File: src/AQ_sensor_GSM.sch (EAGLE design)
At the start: 56 parts, among them IC2 MCP73831/OT, J1 F-1X03-SIP-100-32, SW1 PCM12SMTR, U2 TEXAS_INSTRUMENTS_SN74HC125TE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, U3 TEXAS_INSTRUMENTS_LM1117IMP-3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, U4 ESP8266-12E/ESP-12E, U5 CH340G, X1 53048-08, X2 SIMLOCK-C707_10M006_512_2, X4 50 Ohms

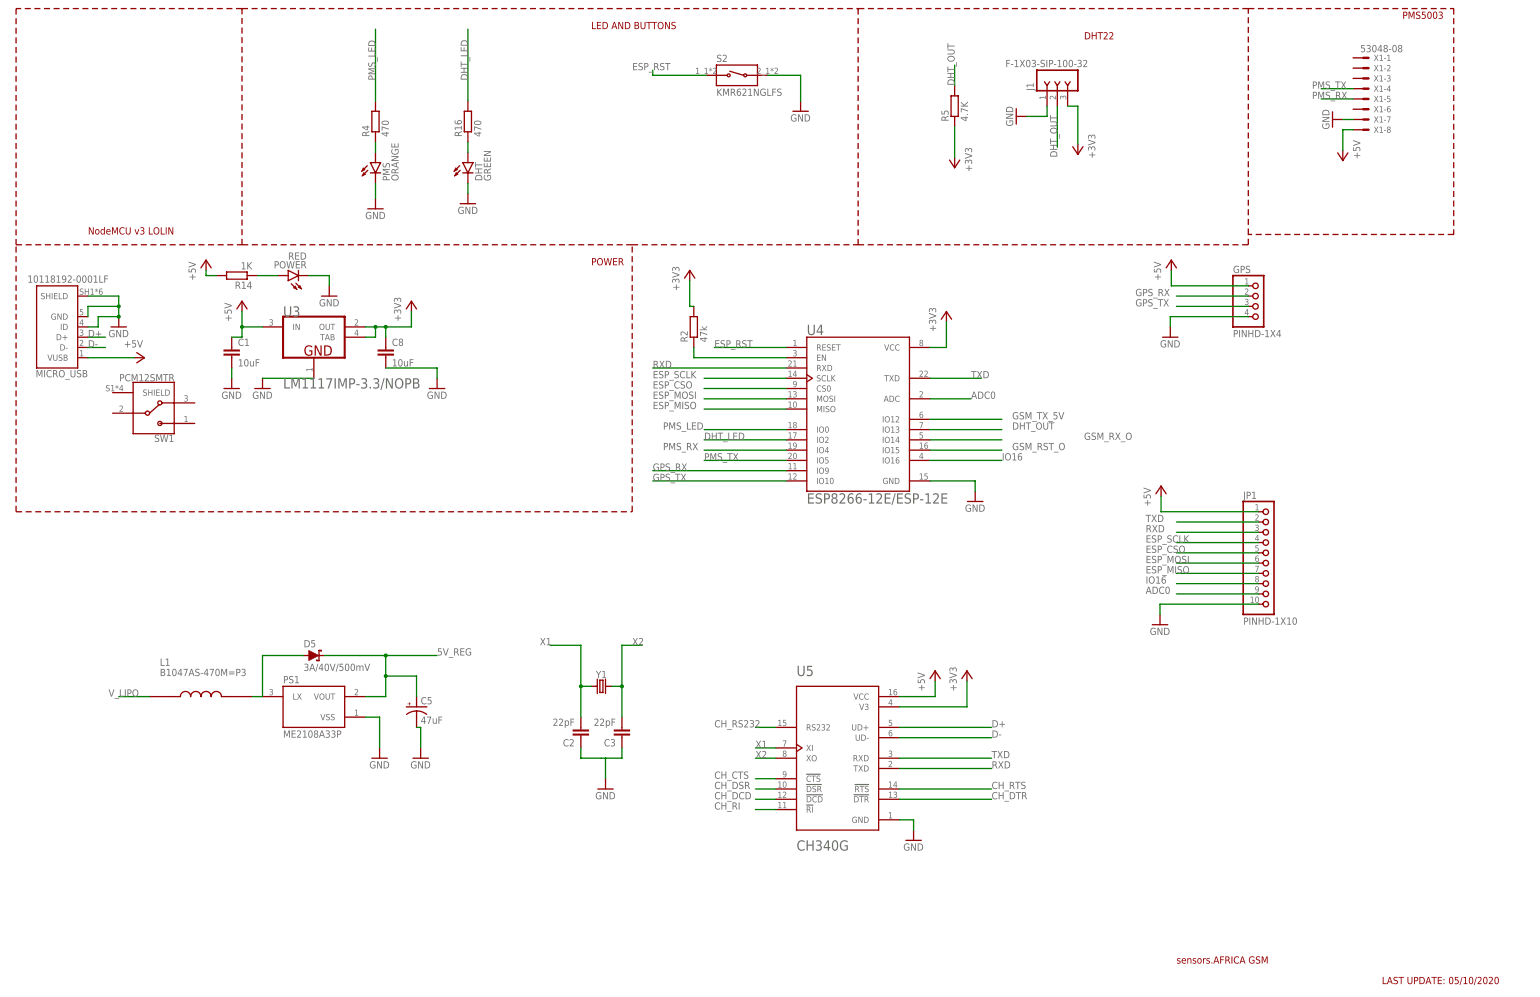
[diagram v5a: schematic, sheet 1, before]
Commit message: Changed Lipo charging IC to TP4056. Added Power Switch to the lipo Circuitry
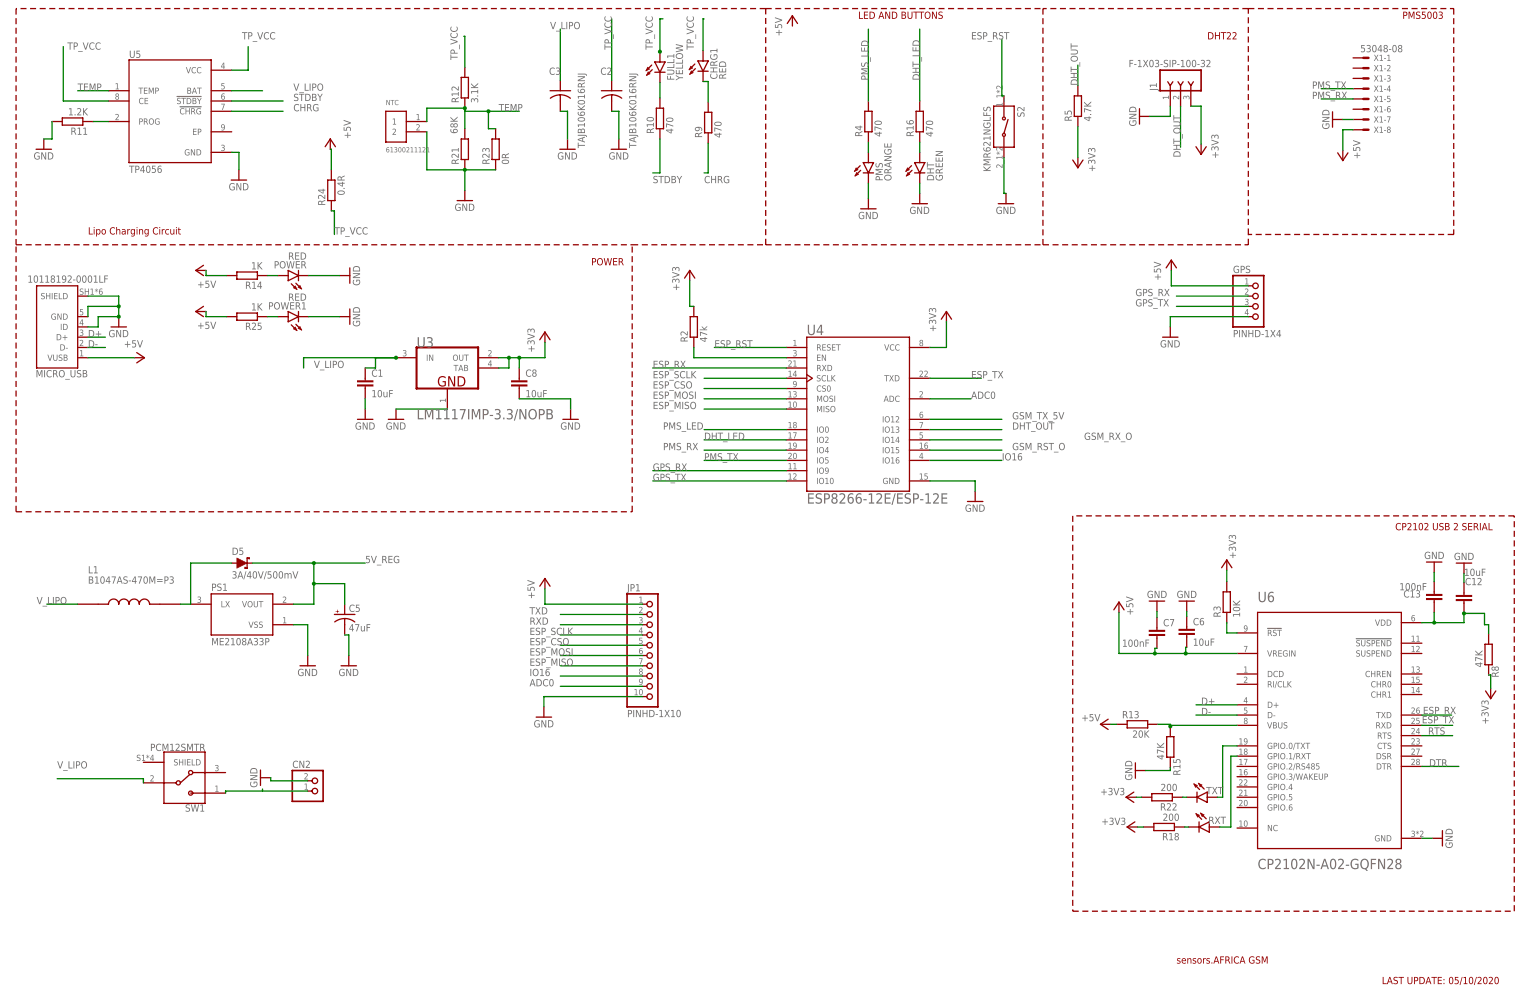
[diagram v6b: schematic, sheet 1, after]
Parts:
- removed Y1: (no value), SparkFun-Clocks:CRYSTALPTH-HC49US
- added C12, C6: 10uF, rcl:C-EUC0603
- added C13, C7: 100nF, rcl:C-EUC0805
- added CHRG1, POWER1: RED, led:LEDCHIP-LED0603
- added CN2: (no value), AQ_sensor_GSM:JST_2PIN-SMT-RA
- added FULL1: YELLOW, led:LEDCHIP-LED0603
- added NTC: 61300211121, Headers:61300211121
- added R10, R9: 470, rcl:R-EU_R0603
- added R11: 1.2K, rcl:R-EU_R0603
- added R12: 3.1K, rcl:R-EU_R0603
- added R13: 20K, rcl:R-EU_R0603
- added R15, R8: 47K, rcl:R-EU_R0603
- added R18, R22: 200, rcl:R-EU_R0603
- added R21: 68K, rcl:R-EU_R0603
- added R23: 0R, rcl:R-EU_R0603
- added R24: 0.4R, rcl:R-EU_R0603
- added R25: 1K, rcl:R-EU_R0603
- added R3: 10K, rcl:R-EU_R0603
- added RXT, TXT: (no value), led:LEDCHIP-LED0603
- added U6: CP2102N-A02-GQFN28, noise_monitor:CP2102N-A02-GQFN28
- C2, C3: value 22pF -> TAJB106K016RNJ; device SparkFun-Capacitors:22PF-0603-50V-5% -> Resistor_Capacitor:TAJB106K016RNJ
- U5: value CH340G -> TP4056; device CH340G (1):CH340G -> TP4056:TP4056
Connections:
- removed net CH_CTS: U5.!CTS
- removed net CH_DCD: U5.!DCD
- removed net CH_DSR: U5.!DSR
- removed net CH_DTR: U5.!DTR
- removed net CH_RI: U5.!RI
- removed net CH_RS232: U5.RS232
- removed net CH_RTS: U5.!RTS
- removed net X1: C2.2, U5.XI, Y1.1
- removed net X2: C3.2, U5.XO, Y1.2
- new net CHRG: R9.1, U5.!CHRG
- new net DTR: U6.DTR
- new net ESP_RX: U4.RXD, U6.TXD
- new net ESP_TX: U4.TXD, U6.RXD
- new net N$15: C12.2, C13.2, R8.1, U6.VDD
- new net N$16: R11.1, U5.PROG
- new net N$17: TXT.A, U6.GPIO.0/TXT
- new net N$18: RXT.A, U6.GPIO.1/RXT
- new net N$19: CHRG1.C, R9.2
- new net N$20: FULL1.C, R10.2
- new net N$21: POWER1.A, R25.1
- new net N$22: CN2.2, SW1.1
- new net N$3: R13.2, R15.1, U6.VBUS
- new net N$5: R3.1, U6.!RST
- new net N$7: R22.1, TXT.C
- new net N$8: R18.1, RXT.C
- new net RTS: U6.RTS
- new net STDBY: R10.1, U5.!STDBY
- new net TEMP: NTC.1, R12.1, R21.2, R23.2, U5.TEMP
- new net TP_VCC: C2.1, CHRG1.A, FULL1.A, R12.2, R24.1, U5.CE, U5.VCC
- net +3V3: now also R18.2, R22.2, R3.2, R8.2; no longer U5.V3
- net +5V: now also C6.2, C7.2, R13.1, R24.2, R25.2, U6.VREGIN; no longer C1.1, U3.IN, U5.VCC
- net D+: now also U6.D+; no longer U5.UD+
- net D-: now also U6.D-; no longer U5.UD-
- net GND: now also C12.1, C13.1, C2.2, C3.2, C6.1, C7.1, CN2.1, NTC.2, POWER1.C, R11.2, R15.2, R21.1, R23.1, U6.GND; no longer C2.1, C3.1
- net RXD: no longer U4.RXD, U5.TXD
- net TXD: no longer U4.TXD, U5.RXD
- net V_LIPO: now also C1.1, C3.1, SW1.2, U3.IN, U5.BAT
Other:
- note added: "CP2102 USB 2 SERIAL"
- note added: "Lipo Charging Circuit"
- note removed: "NodeMCU v3 LOLIN"
- moved on the sheet: C1, C2, C3, C5, C8, D5, DHT, J1, JP1, L1, PMS, PS1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

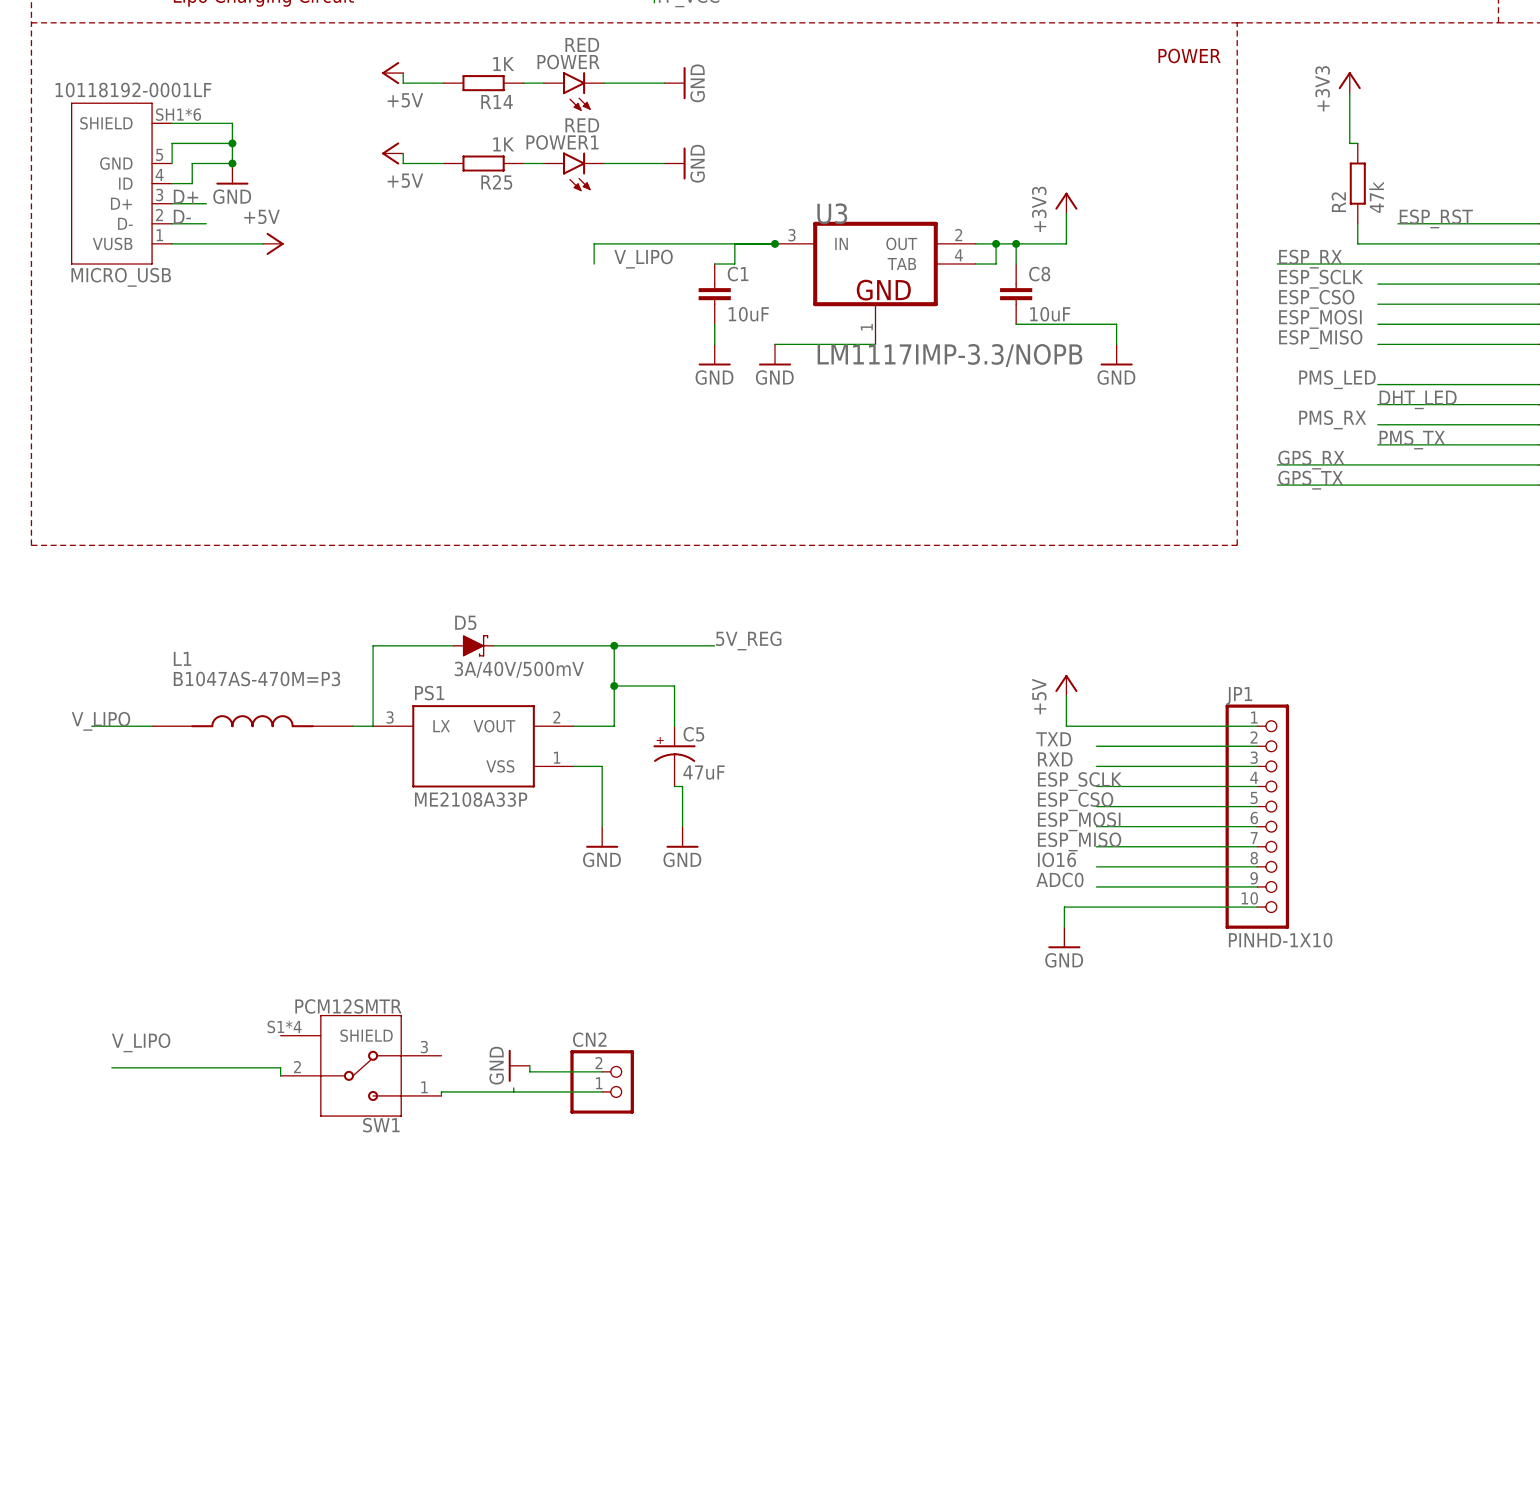
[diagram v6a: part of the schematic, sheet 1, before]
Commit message: Added LC filter to the MT3608 boost circuit
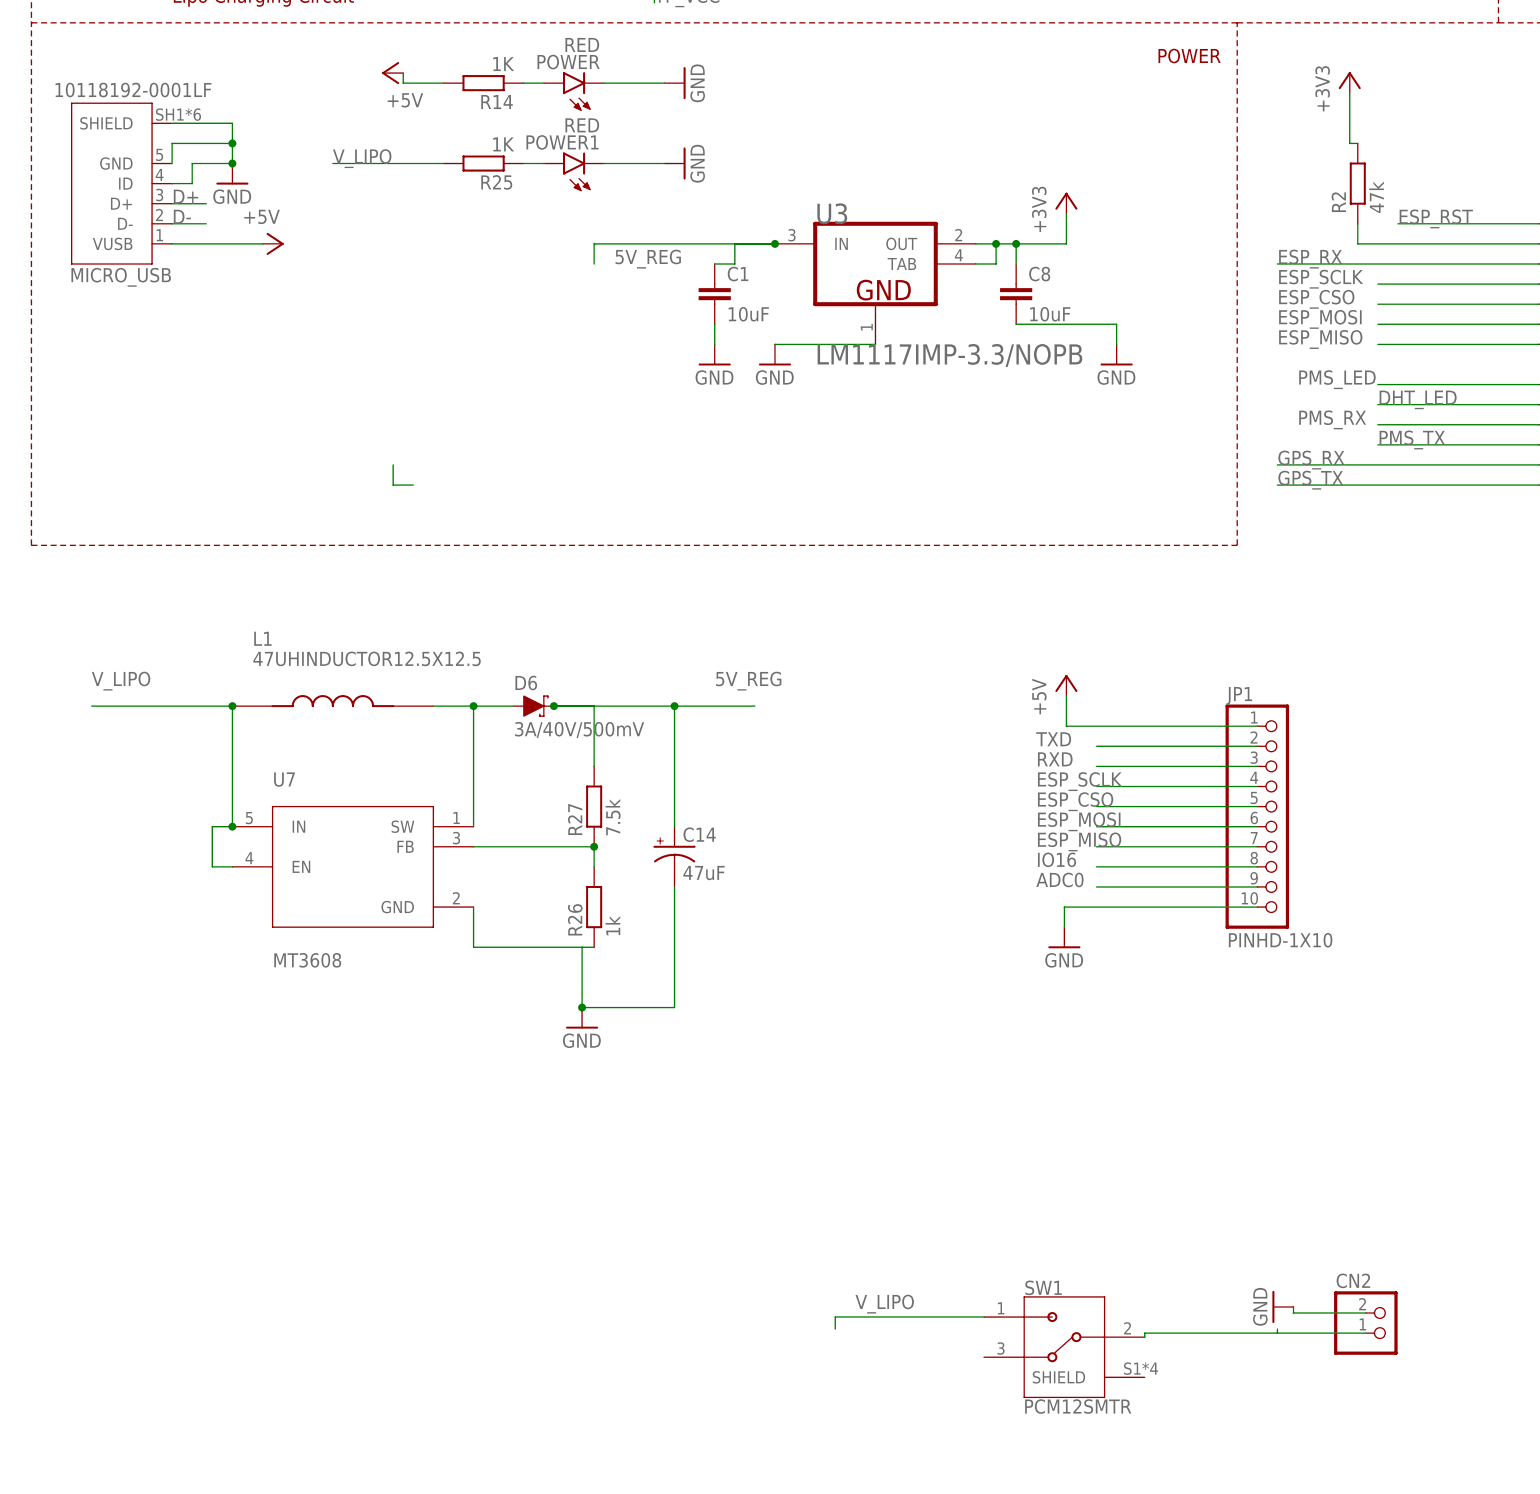
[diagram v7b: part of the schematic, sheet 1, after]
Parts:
- removed C5: 47uF, SparkFun-Capacitors:47UF-POLAR-EIA3528-10V-10%
- removed D5: 3A/40V/500mV, SparkFun-DiscreteSemi:DIODE-SCHOTTKY-B340A
- removed PS1: ME2108A33P, ME2108A33P:ME2108A33P
- added C14: 47uF, SparkFun-Capacitors:47UF-POLAR-EIA3528-10V-10%
- added D6: 3A/40V/500mV, SparkFun-DiscreteSemi:DIODE-SCHOTTKY-B340A
- added R26: 1k, rcl:R-EU_R0603
- added R27: 7.5k, rcl:R-EU_R0603
- added U7: MT3608, MT3608:MT3608
- L1: value B1047AS-470M=P3 -> 47UHINDUCTOR12.5X12.5; device B1047AS-470M_P3:B1047AS-470M=P3 -> 47 uH inductor 12.5X12.5:47UHINDUCTOR12.5X12.5
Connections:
- removed net N$1: D5.A, L1.2, PS1.LX
- new net N$23: D6.A, L1.2, U7.SW
- new net N$26: R26.2, R27.1, U7.FB
- net +5V: no longer R25.2
- net 5V_REG: now also C1.1, C14.+, D6.C, R27.2, U3.IN; no longer C5.+, D5.C, PS1.VOUT
- net GND: now also C14.-, R26.1, U7.GND; no longer C5.-, PS1.VSS
- net N$22: now also SW1.2; no longer SW1.1
- net V_LIPO: now also R25.2, SW1.1, U7.EN, U7.IN; no longer C1.1, SW1.2, U3.IN
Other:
- moved on the sheet: CN2, L1, SW1
